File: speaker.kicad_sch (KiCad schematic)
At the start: 18 parts, among them SW1 SW_DIP_x08

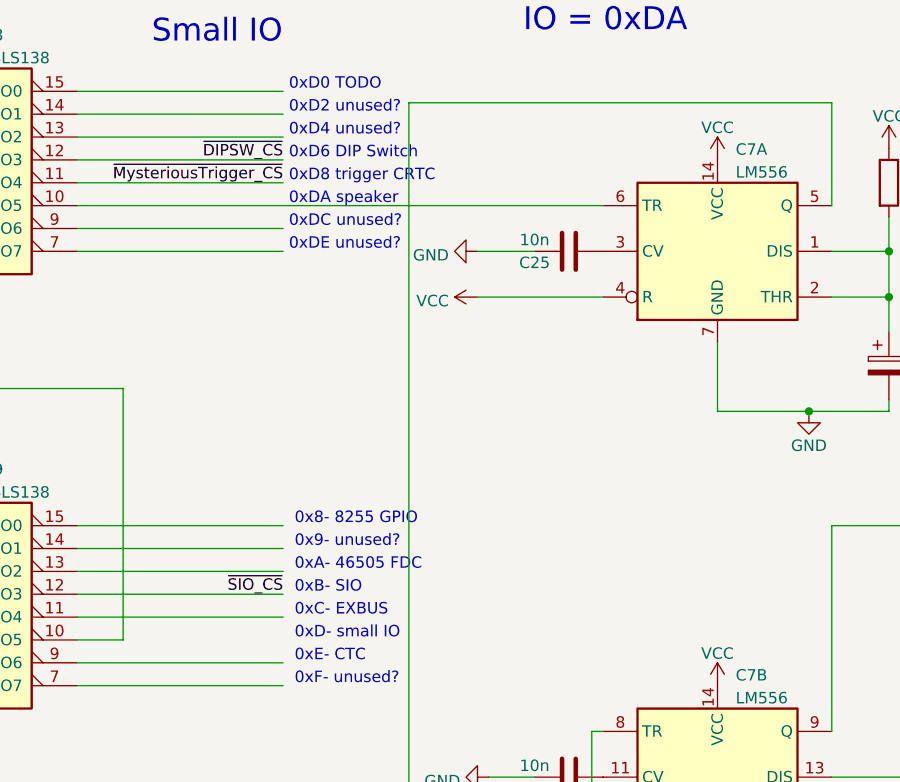
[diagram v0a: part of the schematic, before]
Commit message: Found vsync frame signal for z80 + minors
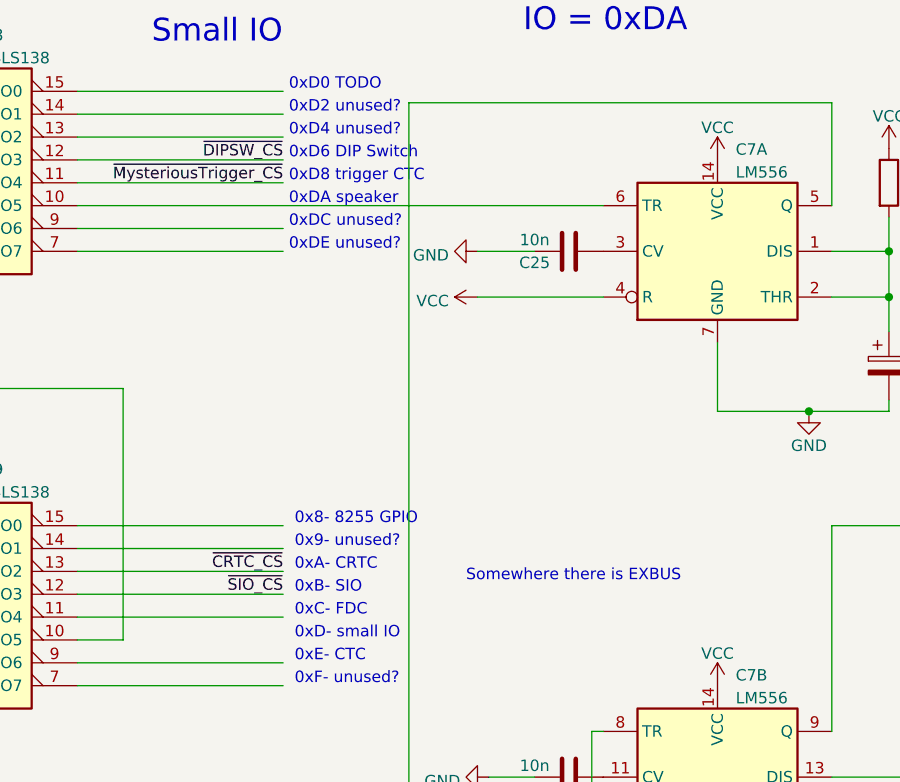
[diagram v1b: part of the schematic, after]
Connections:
- net ~{CRTC_CS}: now reaches D9.13 (O2)
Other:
- note added: "0xA- CRTC"
- note added: "0xC- FDC"
- note added: "0xD8 trigger CTC"
- note added: "Somewhere there is EXBUS"
- note removed: "0xA- 46505 FDC"
- note removed: "0xC- EXBUS"
- note removed: "0xD8 trigger CRTC"
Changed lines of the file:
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@@
     (stroke (width 0) (type default))
+  )
+  (text "Somewhere there is EXBUS" (at 133.35 86.36 0)
+    (effects (font (size 1.27 1.27)) (justify left bottom))
   )
   (text "0xDC unused?" (at 113.665 46.99 0)
@@
     (effects (font (size 1.27 1.27)) (justify left bottom))
   )
-  (text "0xA- 46505 FDC" (at 114.3 85.09 0)
+  (text "0xA- CRTC" (at 114.3 85.09 0)
     (effects (font (size 1.27 1.27)) (justify left bottom))
   )
@@
     (effects (font (size 1.27 1.27)) (justify left bottom))
   )
-  (text "0xD8 trigger CRTC" (at 113.665 41.91 0)
+  (text "0xD8 trigger CTC" (at 113.665 41.91 0)
     (effects (font (size 1.27 1.27)) (justify left bottom))
   )
@@
     (effects (font (size 1.27 1.27)) (justify left bottom))
   )
-  (text "0xC- EXBUS" (at 114.3 90.17 0)
+  (text "0xC- FDC" (at 114.3 90.17 0)
     (effects (font (size 1.27 1.27)) (justify left bottom))
   )
@@
     (effects (font (size 1.27 1.27)) (justify left bottom))
   )
+  (label "~{CRTC_CS}" (at 113.03 85.09 180) (fields_autoplaced)
+    (effects (font (size 1.27 1.27)) (justify right bottom))
+  )
   (label "addr3" (at 59.69 36.83 0) (fields_autoplaced)

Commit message: CTC, serial clock and main clock
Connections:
- net ~{CTC_CS}: now reaches D9.9 (O6)
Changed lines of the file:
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@@
     (effects (font (size 1.27 1.27)) (justify left bottom))
+  )
+  (label "~{CTC_CS}" (at 113.03 95.25 180) (fields_autoplaced)
+    (effects (font (size 1.27 1.27)) (justify right bottom))
   )
   (label "~{RD}" (at 67.31 173.99 0) (fields_autoplaced)

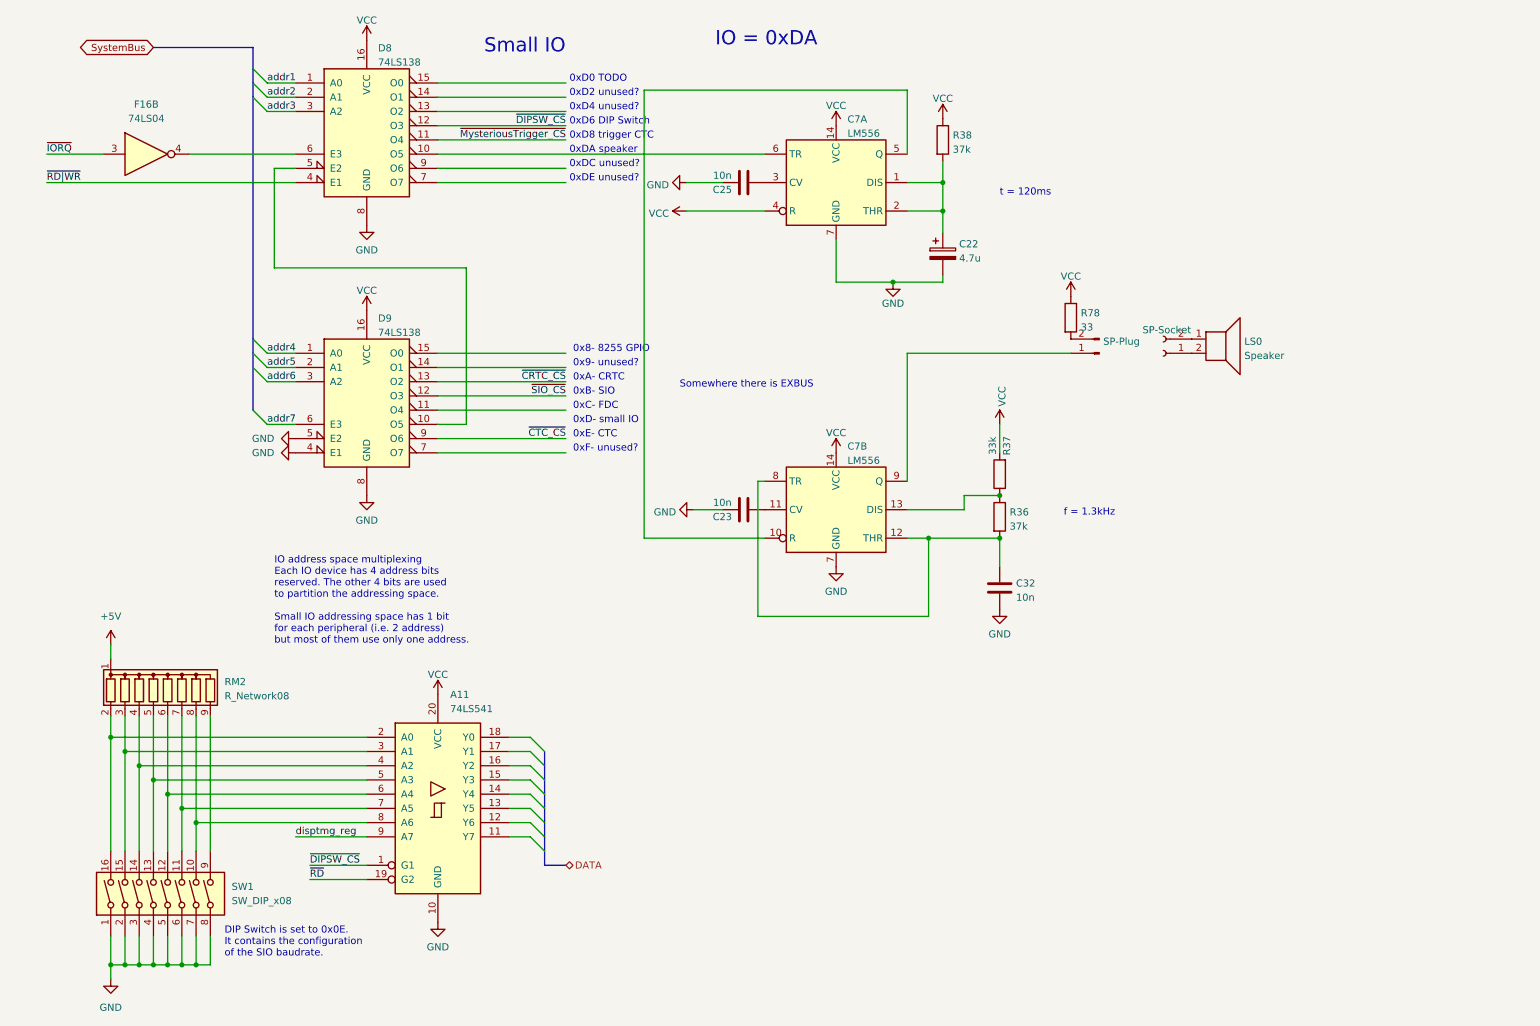
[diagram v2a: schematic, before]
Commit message: Schematics refactoring:
- New sheet reserved to video memory.
- Removed video memory parts inside video_generation.
- Removed video memory parts inside GPIO.
- Generic cleanup to keep all circuits inside each sheet.
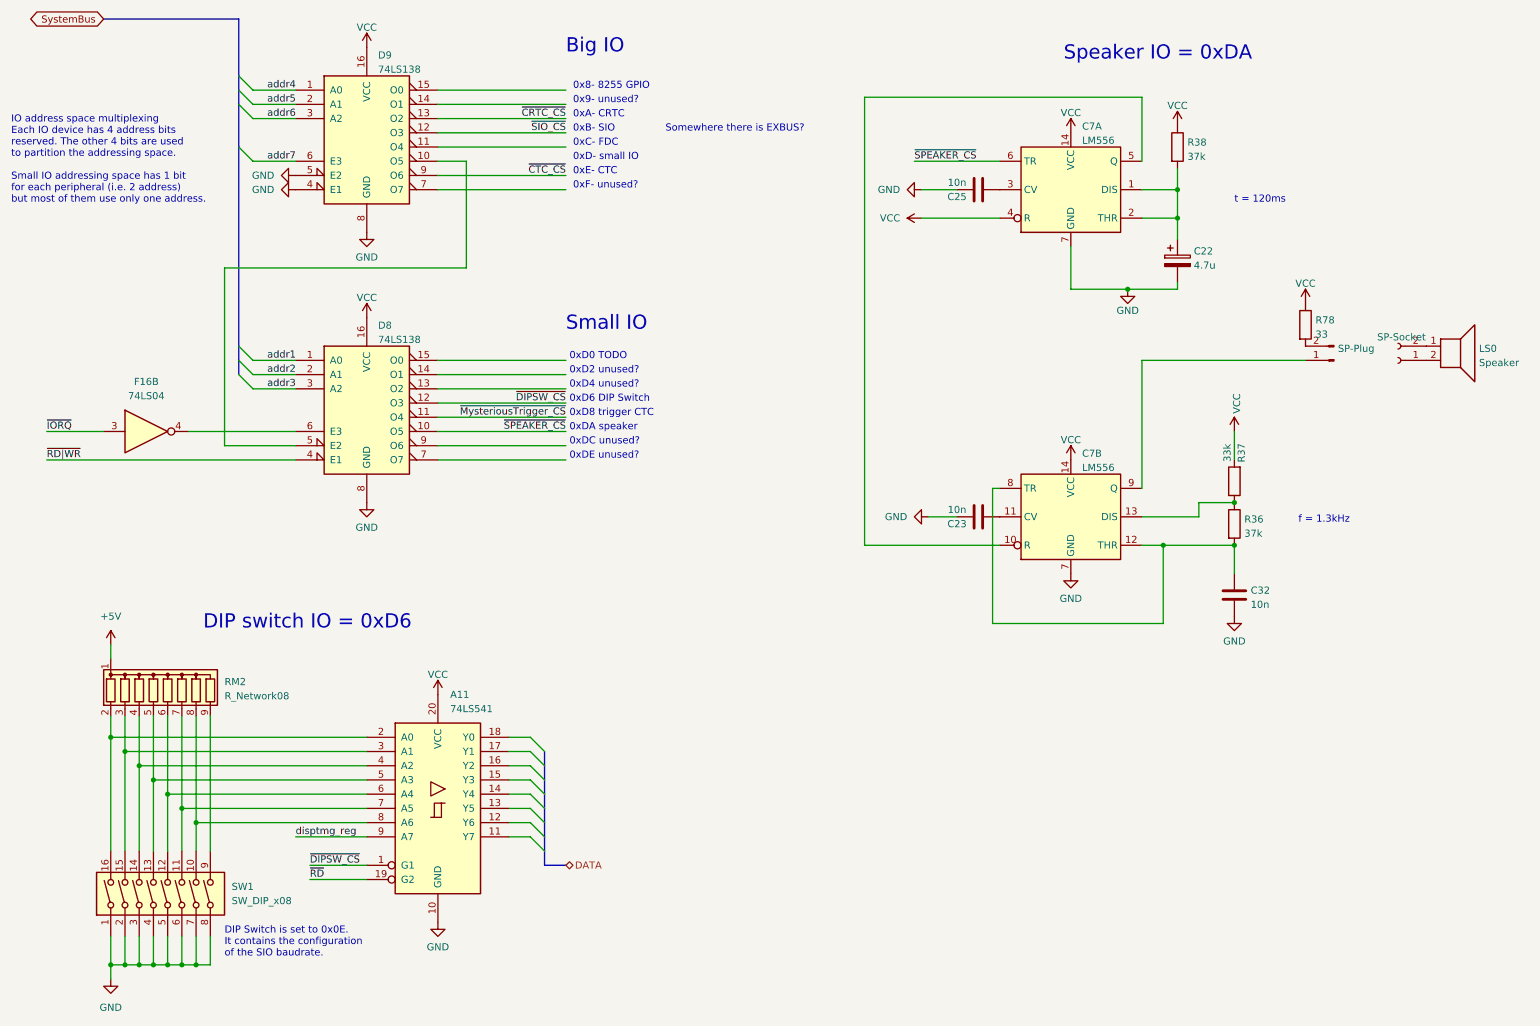
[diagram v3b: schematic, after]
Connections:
- net ~{SPEAKER_CS}: now reaches C7.6 (TR), D8.10 (O5)
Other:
- note added: "Big IO"
- note added: "DIP switch IO = 0xD6"
- note added: "Somewhere there is EXBUS?"
- note added: "Speaker IO = 0xDA"
- note removed: "IO = 0xDA"
- note removed: "Somewhere there is EXBUS"
- moved on the sheet: C22, C23, C25, C32, C7A, C7B, D8, D9, F16B, LS0, R36, R37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

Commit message: IO space: wire renaming
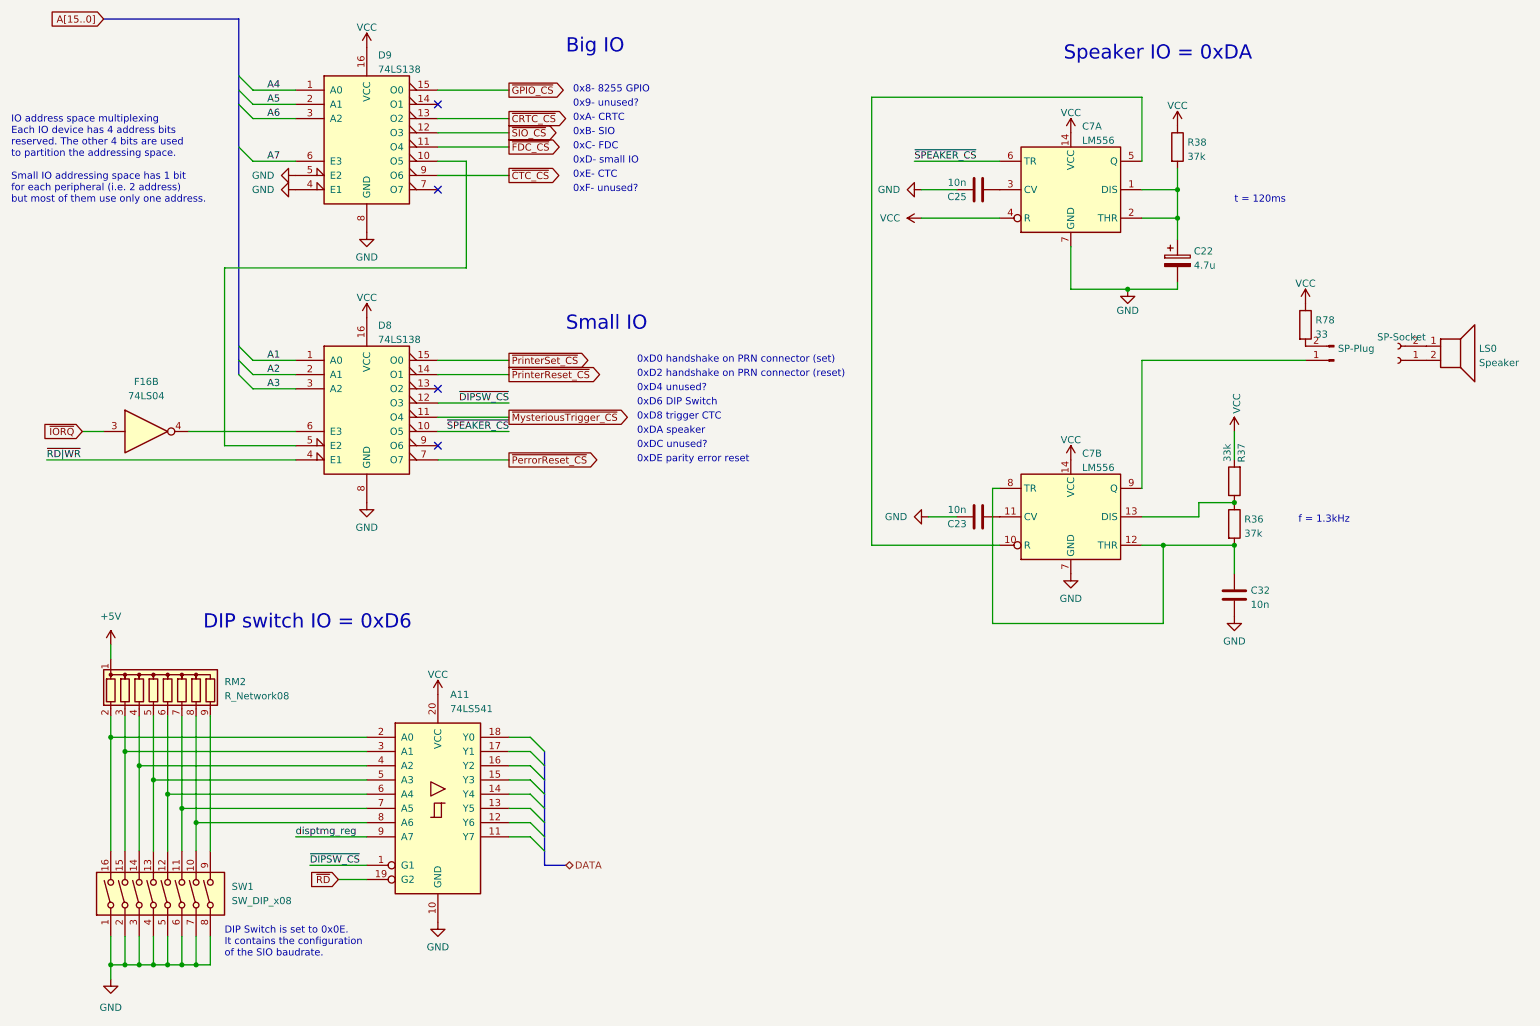
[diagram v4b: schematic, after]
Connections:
- net ~{PrinterReset_CS}: now reaches D8.14 (O1)
- net ~{PrinterSet_CS}: now reaches D8.15 (O0)
- net ~{PerrorReset_CS}: now reaches D8.7 (O7)
- net ~{FDC_CS}: now reaches D9.11 (O4)
- net ~{GPIO_CS}: now reaches D9.15 (O0)
- net addr1 renamed A1
- net addr2 renamed A2
- net addr3 renamed A3
- net addr4 renamed A4
- net addr5 renamed A5
- net addr6 renamed A6
- net addr7 renamed A7
- no-connect marks 0 -> 4
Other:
- note added: "0xD0 handshake on PRN connector (set)"
- note added: "0xD2 handshake on PRN connector (reset)"
- note added: "0xDE parity error reset"
- note removed: "0xD0 TODO"
- note removed: "0xD2 unused?"
- note removed: "0xDE unused?"
- note removed: "Somewhere there is EXBUS?"
